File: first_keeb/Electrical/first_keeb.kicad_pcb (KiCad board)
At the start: 2 copper layers, 95.4 x 72.4 mm, 19 parts, among them SW1 SW_SPST_3x3, SW2 SW_SPST_3x3, U1 RPi_Pico_SMD_TH

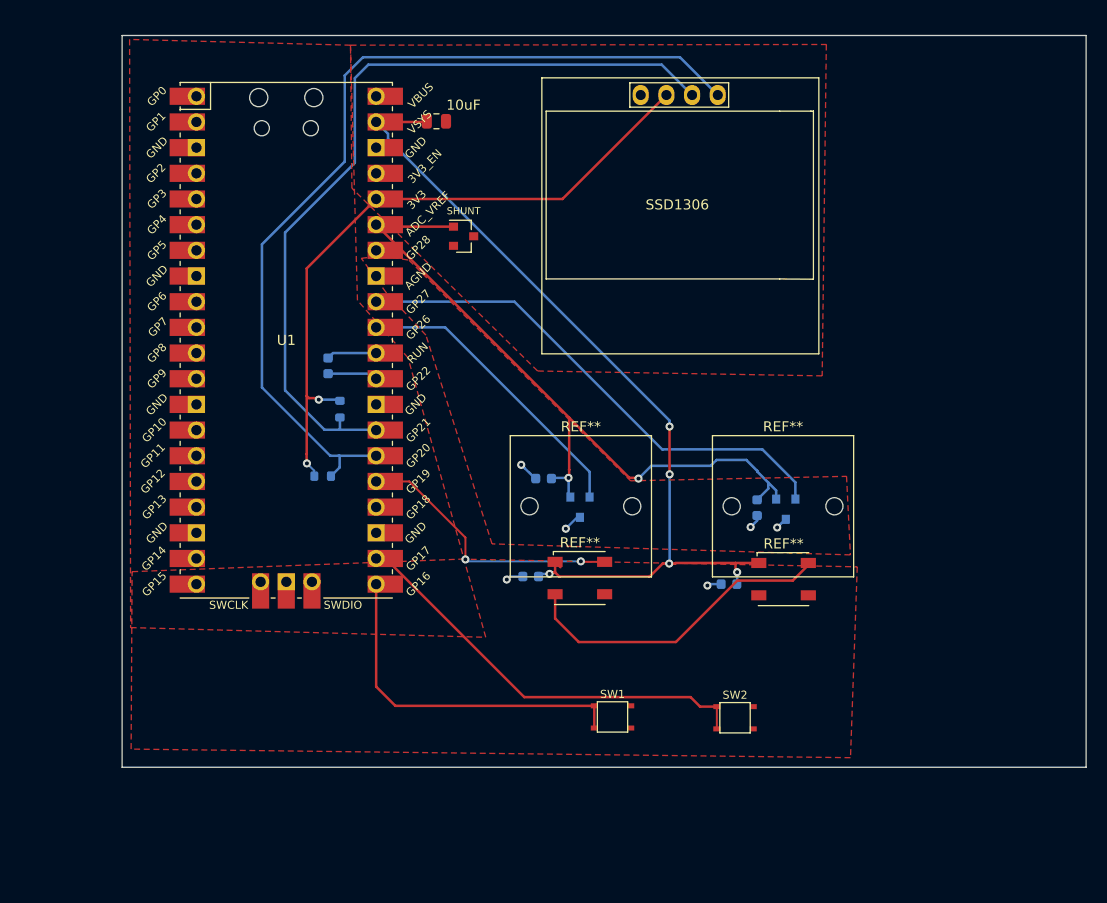
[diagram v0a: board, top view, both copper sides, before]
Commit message: adds right angle switch to pcb and plots gerbers
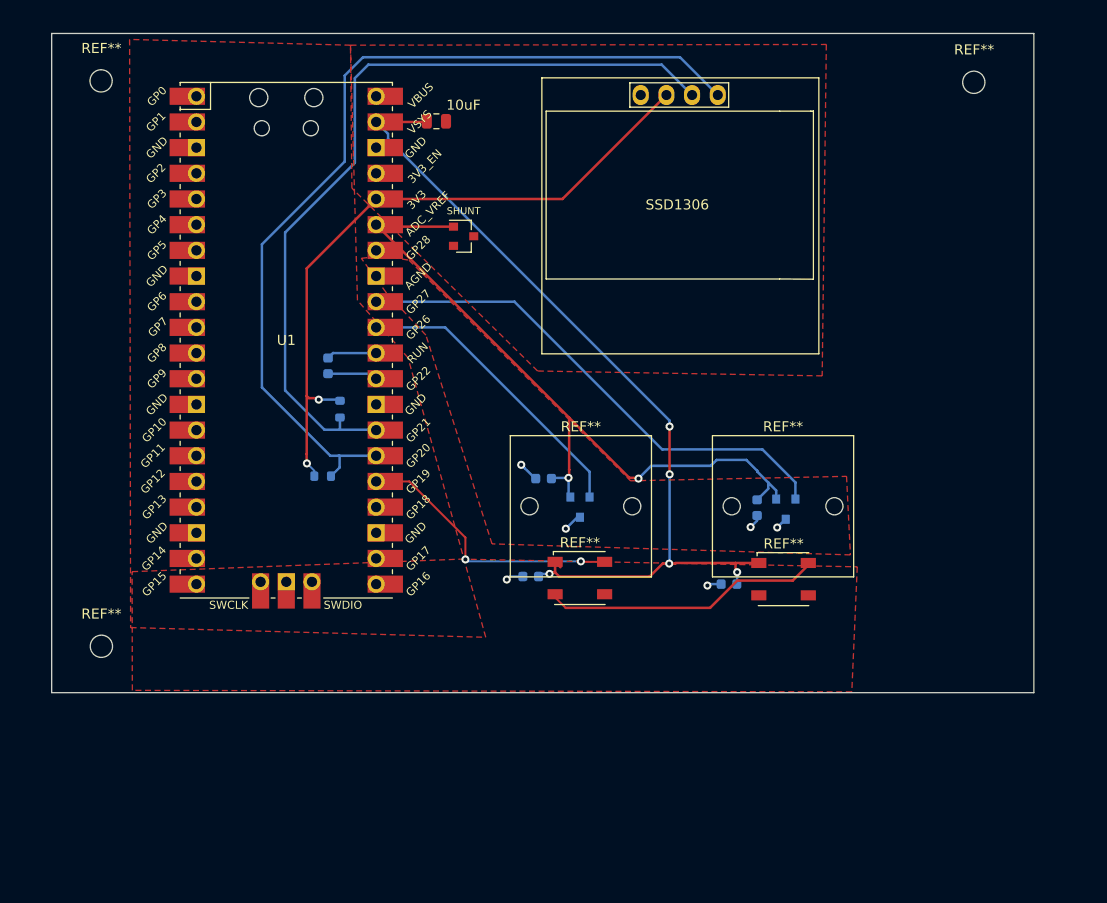
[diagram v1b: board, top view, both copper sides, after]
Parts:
- removed SW1, SW2: SW_SPST_3x3, Keebio-Parts:SW_SPST_3x3
- added REF**: MountingHole_2.2mm_M2, MountingHole:MountingHole_2.2mm_M2, F.Cu at (25.0, 63.0)
- added REF**: MountingHole_2.2mm_M2, MountingHole:MountingHole_2.2mm_M2, F.Cu at (111.4, 63.1)
- added REF**: MountingHole_2.2mm_M2, MountingHole:MountingHole_2.2mm_M2, F.Cu at (25.0, 118.9)
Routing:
- net (no net): track 625.0 -> 545.3 mm
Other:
- board size 95.4 x 72.4 mm -> 97.2 x 65.2 mm

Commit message: improve pcb
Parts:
- added REF**: MountingHole_2.2mm_M2, MountingHole:MountingHole_2.2mm_M2, F.Cu at (105.0, 125.0)
- added REF**: 2-1825027-0_Right_Angle_Switch-9.24mm_Stem, Button_Switch_THT:2-1825027-0_Right_Angle_Button, F.Cu at (86.0, 124.9)
- added REF**: 2-1825027-0_Right_Angle_Switch-9.24mm_Stem, Button_Switch_THT:2-1825027-0_Right_Angle_Button, F.Cu at (65.5, 124.9)
- moved REF** 9.74 mm to (105.0, 70.5)
- moved REF** 7.65 mm to (23.5, 70.5)
- moved SSD1306 6.80 mm to (78.8, 81.0)
- moved REF** 6.26 mm to (23.5, 125.0)
- moved PULL 4.47 mm to (43.7, 105.2)
- moved RST 4.47 mm to (44.2, 94.3)
- moved CUP 4.47 mm to (64.3, 115.1)
- moved REF** 4.47 mm to (89.5, 108.5)
- moved REF** 4.47 mm to (89.3, 115.4)
- moved SENS 4.47 mm to (69.2, 108.3)
- moved 10uF 4.47 mm to (55.0, 70.1)
- moved PULL 4.47 mm to (45.4, 98.6)
- moved SHUNT 4.47 mm to (57.6, 81.5)
- moved U1 4.47 mm to (40.1, 91.8)
- moved CUP 4.47 mm to (83.9, 115.9)
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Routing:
- net (no net): track 545.3 -> 559.3 mm
- net GND: track 3.13 -> 7.09 mm, vias 2 -> 4
- net AGND: track 5.52 -> 7.71 mm
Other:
- board size 97.2 x 65.2 mm -> 91.5 x 64.5 mm

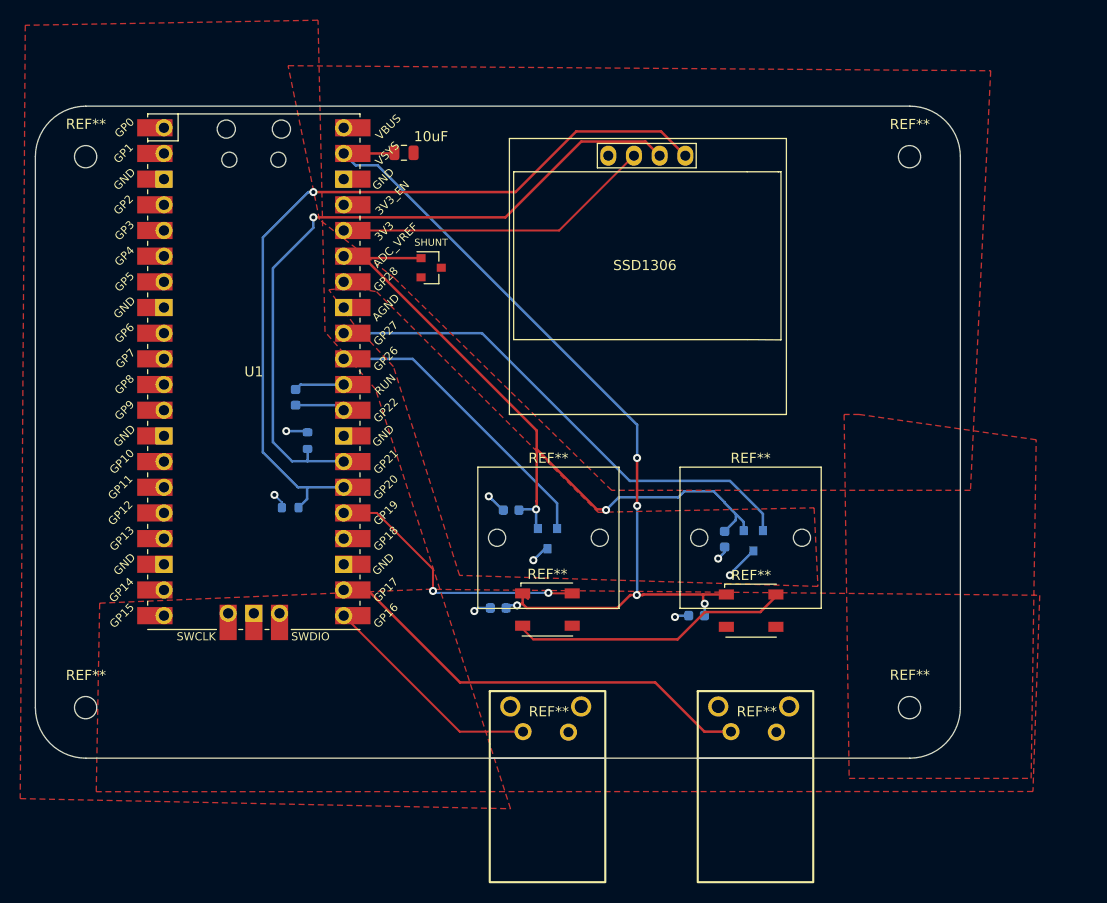
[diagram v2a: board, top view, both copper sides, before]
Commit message: add gnd pour on back layer
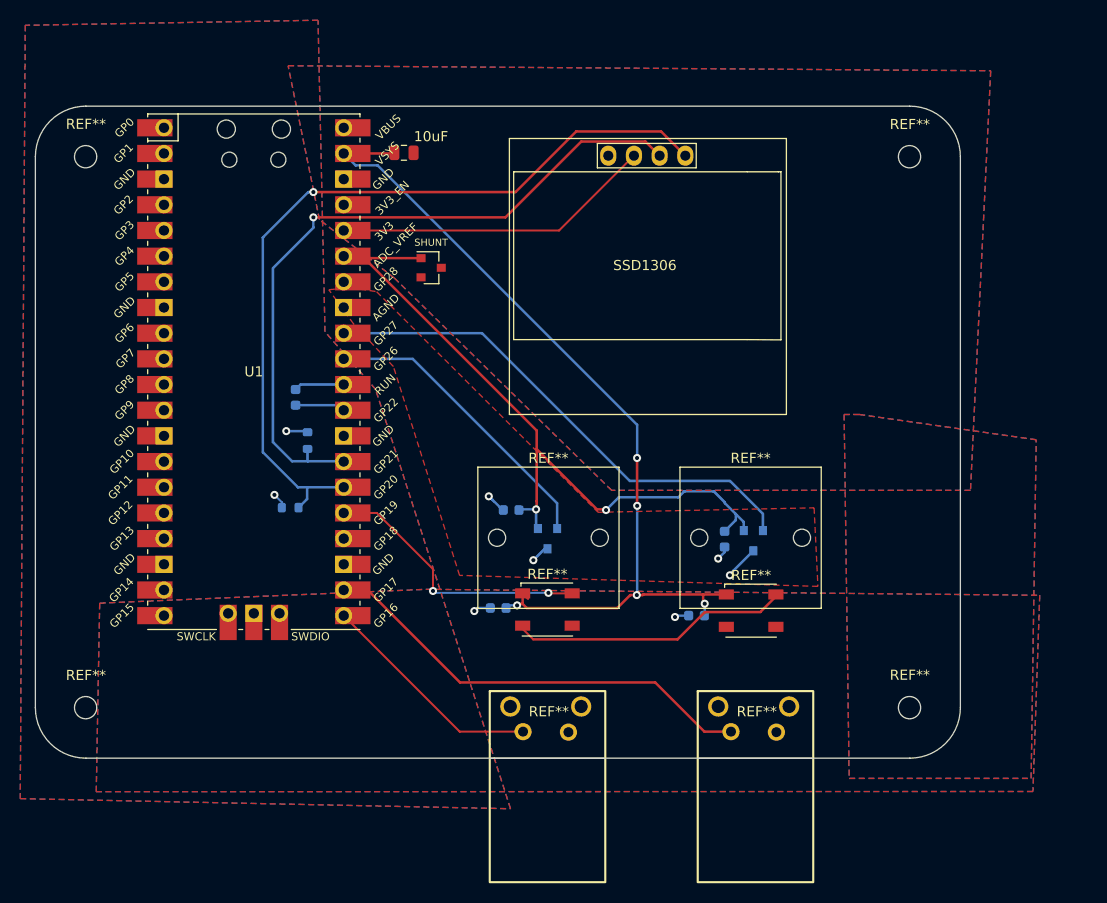
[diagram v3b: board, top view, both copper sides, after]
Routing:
- added copper zone on B.Cu, net GND
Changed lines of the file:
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@@
   (segment (start 62.22 115.145) (end 61.92 115.445) (width 0.25) (layer "B.Cu") (net 2))
   (segment (start 81.91 115.895) (end 81.77 116.035) (width 0.25) (layer "B.Cu") (net 2))
-  (zone (net 2) (net_name "GND") (layer "F.Cu") (hatch edge 0.5)
-    (priority 2)
-    (connect_pads (clearance 0.508))
-    (min_thickness 0.25) (filled_areas_thickness no)
-    (fill yes (thermal_gap 0.5) (thermal_bridge_width 0.5) (island_removal_mode 1) (island_area_min 10))
-    (polygon
-      (pts
-        (xy 17.5 57.5)
-        (xy 17 134)
-        (xy 65.5 135)
-        (xy 52.15 93.505)
-        (xy 47.15 87.825)
-        (xy 46.46 57)
-      )
-    )
-  )
   (zone (net 1) (net_name "AGND") (layer "F.Cu") (hatch edge 0.5)
     (connect_pads (clearance 0.508))
@@
     )
   )
-  (zone (net 2) (net_name "GND") (layer "F.Cu") (hatch edge 0.5)
+  (zone (net 2) (net_name "GND") (layers "F&B.Cu") (hatch edge 0.5)
+    (priority 2)
+    (connect_pads (clearance 0.508))
+    (min_thickness 0.25) (filled_areas_thickness no)
+    (fill yes (thermal_gap 0.5) (thermal_bridge_width 0.5) (island_removal_mode 1) (island_area_min 10))
+    (polygon
+      (pts
+        (xy 17.5 57.5)
+        (xy 17 134)
+        (xy 65.5 135)
+        (xy 52.15 93.505)
+        (xy 47.15 87.825)
+        (xy 46.46 57)
+      )
+    )
+  )
+  (zone (net 2) (net_name "GND") (layers "F&B.Cu") (hatch edge 0.5)
     (priority 4)
     (connect_pads (clearance 0.508))
@@
     )
   )
-  (zone (net 2) (net_name "GND") (layer "F.Cu") (hatch edge 0.5)
+  (zone (net 2) (net_name "GND") (layers "F&B.Cu") (hatch edge 0.5)
     (priority 3)
     (connect_pads (clearance 0.508))
@@
     )
   )
-  (zone (net 2) (net_name "GND") (layer "F.Cu") (hatch edge 0.5)
+  (zone (net 2) (net_name "GND") (layers "F&B.Cu") (hatch edge 0.5)
     (priority 1)
     (connect_pads (clearance 0.508))
